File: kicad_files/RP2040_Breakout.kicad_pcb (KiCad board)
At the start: 2 copper layers, 20.8 x 52.3 mm, 4 parts, among them IC1 RPI_Chip_RP2040-10-10, IC3 W25Q128JVSIQ, J1 690-005-298-486, J2 Conn_02x20_Counter_Clockwise

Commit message: placement completed
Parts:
- added C1: 0.1uf, Capacitor_SMD:C_0201_0603Metric, F.Cu at (135.6, 95.6)
- added C10: 0.1uf, Capacitor_SMD:C_0201_0603Metric, F.Cu at (132.1, 97.9)
- added C11: 47uf, Capacitor_SMD:C_0805_2012Metric, F.Cu at (139.8, 90.1)
- added C12: 47uf, Capacitor_SMD:C_0805_2012Metric, F.Cu at (139.7, 84.3)
- added C13: 15pf, Capacitor_SMD:C_0201_0603Metric, F.Cu at (131.9, 109.5)
- added C14: 15pf, Capacitor_SMD:C_0201_0603Metric, F.Cu at (139.8, 108.5)
- added C15: 2u2, Capacitor_SMD:C_0201_0603Metric, F.Cu at (140.7, 95.6)
- added C16: 100nf, Capacitor_SMD:C_0201_0603Metric, F.Cu at (132.1, 91.8)
- added C17: 2u2, Capacitor_SMD:C_0402_1005Metric, F.Cu at (131.2, 92.0)
- added C18: 1nf, Capacitor_SMD:C_0402_1005Metric, F.Cu at (139.5, 93.8)
- added C2: 0.1uf, Capacitor_SMD:C_0201_0603Metric, F.Cu at (138.3, 105.8)
- added C3: 0.1uf, Capacitor_SMD:C_0201_0603Metric, F.Cu at (137.2, 95.6)
- added C4: 0.1uf, Capacitor_SMD:C_0201_0603Metric, F.Cu at (142.3, 97.9)
- added C5: 0.1uf, Capacitor_SMD:C_0201_0603Metric, F.Cu at (142.3, 101.5)
- added C6: 0.1uf, Capacitor_SMD:C_0201_0603Metric, F.Cu at (139.2, 105.8)
- added C7: 0.1uf, Capacitor_SMD:C_0201_0603Metric, F.Cu at (136.4, 95.6)
- added C8: 0.1uf, Capacitor_SMD:C_0201_0603Metric, F.Cu at (139.9, 95.6)
- added C9: 0.1uf, Capacitor_SMD:C_0201_0603Metric, F.Cu at (132.1, 101.5)
- added D1: MBR120VLSFT1G, SamacSys_Parts:SODFL3616X98N, F.Cu at (143.1, 82.9)
- added D2: LED_Small, LED_SMD:LED_0402_1005Metric, F.Cu at (131.7, 81.6)
- added G***: LOGO, footprints:logo2, F.Cu at (136.8, 117.3)
- added IC2: RT6150B-33GQW, SamacSys_Parts:SON50P250X250X80-11N-D, F.Cu at (139.4, 87.0)
- added J3: Conn_01x03_Pin, footprints:3Pin_Header, F.Cu at (137.1, 125.8)
- added L1: 2u2, SamacSys_Parts:DFE2016CKA1R0MP2, F.Cu at (142.8, 87.1)
- added Q1: DMG1012T-7, SamacSys_Parts:SOT50P160X80-3N, F.Cu at (142.4, 93.0)
- added R1: 5.6K, Resistor_SMD:R_0201_0603Metric, F.Cu at (142.5, 99.5)
- added R10: 1R, Resistor_SMD:R_0201_0603Metric, F.Cu at (141.6, 95.6)
- added R11: 200, Resistor_SMD:R_0201_0603Metric, F.Cu at (142.5, 95.6)
- added R12: 1K, Resistor_SMD:R_0201_0603Metric, F.Cu at (136.6, 83.5)
- added R13: DNP, Resistor_SMD:R_0201_0603Metric, F.Cu at (132.8, 95.5)
- added R14: 200K, Resistor_SMD:R_0201_0603Metric, F.Cu at (140.5, 92.2)
- added R15: 100K, Resistor_SMD:R_0201_0603Metric, F.Cu at (140.5, 93.7)
- added R2: 10K, Resistor_SMD:R_0201_0603Metric, F.Cu at (142.5, 100.3)
- added R3: 100K, Resistor_SMD:R_0201_0603Metric, F.Cu at (139.7, 81.8)
- added R4: 100K, Resistor_SMD:R_0201_0603Metric, F.Cu at (139.7, 82.6)
- added R5: 27, Resistor_SMD:R_0201_0603Metric, F.Cu at (138.1, 95.6)
- added R6: 27, Resistor_SMD:R_0201_0603Metric, F.Cu at (138.9, 95.6)
- added R7: R_Small, Resistor_SMD:R_0201_0603Metric, F.Cu at (135.6, 106.0)
- added R8: 1K, Resistor_SMD:R_0201_0603Metric, F.Cu at (137.1, 106.0)
- added R9: 470, Resistor_SMD:R_0402_1005Metric, F.Cu at (133.8, 81.6)
- added REF**: CE-Logo_8.5x6mm_SilkScreen, Symbol:CE-Logo_8.5x6mm_SilkScreen, B.Cu at (137.1, 105.5)
- added REF**: FCC-Logo_7.3x6mm_SilkScreen, Symbol:FCC-Logo_7.3x6mm_SilkScreen, B.Cu at (136.6, 113.8)
- added S1: PTS815_SJM_250_SMTR_LFS, SamacSys_Parts:PTS815SJM250SMTRLFS, F.Cu at (133.2, 86.4)
- added TP1: , footprints:Custom_testpad, B.Cu at (139.4, 83.1)
- added TP2: , footprints:Custom_testpad, B.Cu at (139.4, 85.4)
- added TP3: , footprints:Custom_testpad, B.Cu at (139.4, 87.8)
- added TP4: , footprints:Custom_testpad, B.Cu at (139.4, 90.1)
- added TP5: , footprints:Custom_testpad, B.Cu at (134.6, 83.1)
- added TP6: , footprints:Custom_testpad, B.Cu at (134.6, 85.4)
- added Y1: Crystal_GND23, SamacSys_Parts:YSX321SL, F.Cu at (136.4, 109.0)
- IC3: value W25Q128JVSIQ -> W25Q16JVUXIQ_TR; footprint SamacSys_Parts:SOIC127P790X216-8N -> SamacSys_Parts:SON50P300X200X60-9N
- moved IC3 43.1 mm to (133.9, 92.9), turned to 90 degrees
- moved IC1 2.64 mm to (137.1, 100.5)
- moved J1 1.15 mm to (137.1, 76.9)
- moved J2 0.65 mm to (137.1, 100.5)
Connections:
- IC3 pad 1: unconnected-(IC3-/CS-Pad1) -> /rp2040/QSPI_SS_N
- IC3 pad 2: unconnected-(IC3-DO_(IO1)-Pad2) -> /rp2040/QSPI_SD1
- IC3 pad 3: unconnected-(IC3-/WP_(IO2)-Pad3) -> /rp2040/QSPI_SD2
- IC3 pad 4: unconnected-(IC3-GND-Pad4) -> GND
- IC3 pad 5: unconnected-(IC3-DI_(IO0)-Pad5) -> /rp2040/QSPI_SD0
- IC3 pad 6: unconnected-(IC3-CLK-Pad6) -> /rp2040/QSPI_SCLK
- IC3 pad 7: unconnected-(IC3-/HOLD_OR_/RESET_(IO3)-Pad7) -> /rp2040/QSPI_SD3
- IC3 pad 8: unconnected-(IC3-VCC-Pad8) -> /rp2040/IOVDD_1
- J1 pad SH1: (no net) -> GND
- J1 pad SH2: (no net) -> GND
- J1 pad SH3: (no net) -> GND
- J1 pad SH4: (no net) -> GND
- J1 pad SH5: (no net) -> GND
- J1 pad SH6: (no net) -> GND
- J2 pad 36: /power_chain/3V3 -> /rp2040/IOVDD_1
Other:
- board size 20.8 x 52.3 mm -> 21 x 52.3 mm

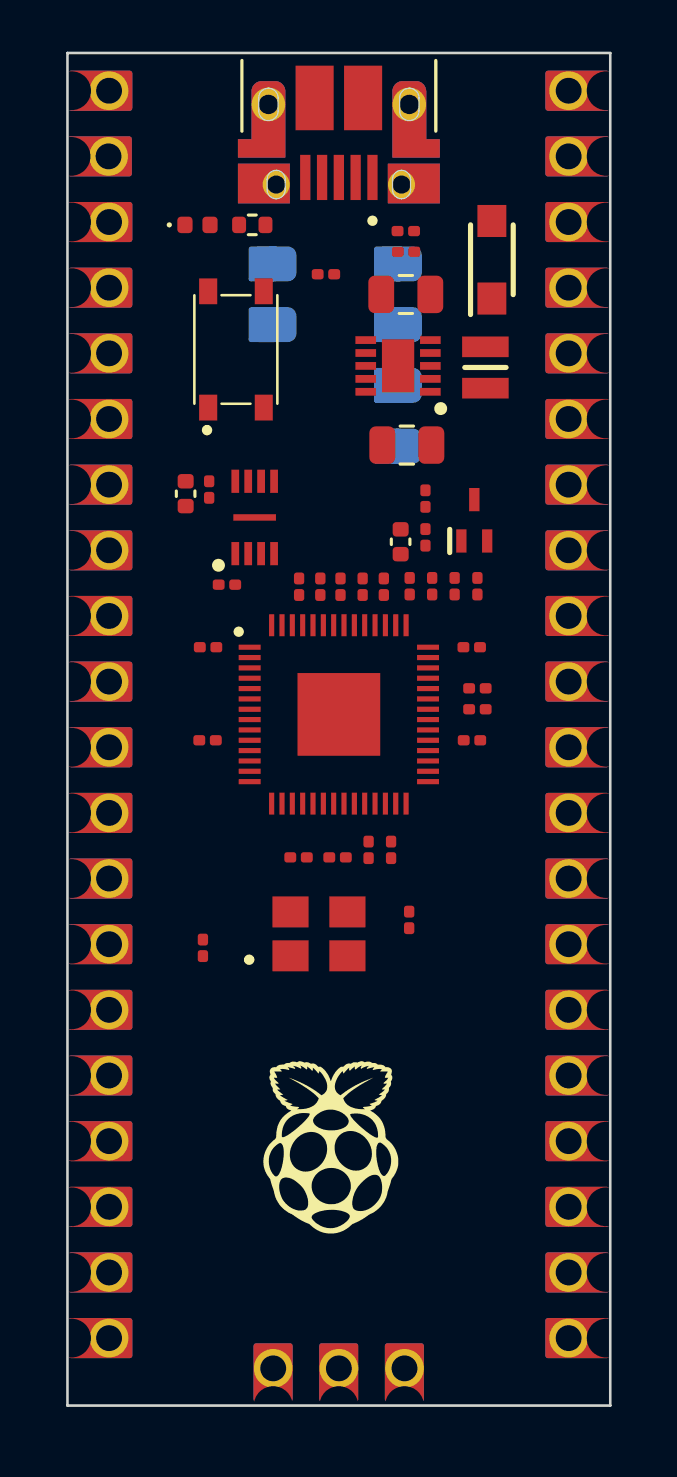
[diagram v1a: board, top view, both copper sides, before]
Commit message: initial routing started
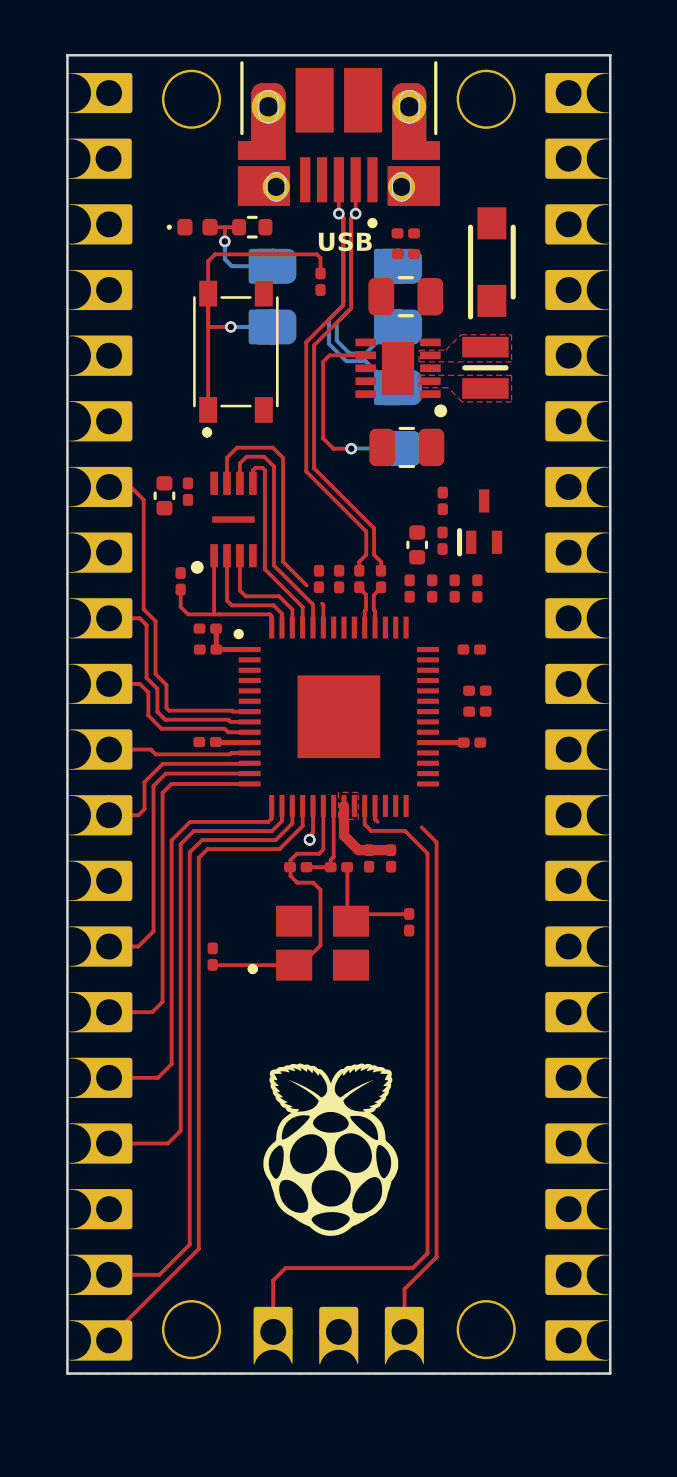
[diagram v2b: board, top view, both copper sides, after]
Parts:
- removed REF**: CE-Logo_8.5x6mm_SilkScreen, Symbol:CE-Logo_8.5x6mm_SilkScreen
- removed REF**: FCC-Logo_7.3x6mm_SilkScreen, Symbol:FCC-Logo_7.3x6mm_SilkScreen
- added H1: MountingHole, footprints:Mounting_Hole, F.Cu at (131.4, 76.7)
- added H2: MountingHole, footprints:Mounting_Hole, F.Cu at (142.8, 76.7)
- added H3: MountingHole, footprints:Mounting_Hole, F.Cu at (131.4, 124.3)
- added H4: MountingHole, footprints:Mounting_Hole, F.Cu at (142.8, 124.3)
- moved C1 3.89 mm to (132.1, 97.2), turned to 180 degrees
- moved R13 1.79 mm to (131.0, 95.4), turned to 90 degrees
- moved J3 1.41 mm to (137.1, 124.4)
- moved C16 0.82 mm to (131.3, 91.9)
- moved C17 0.82 mm to (130.4, 92.1)
- moved IC3 0.82 mm to (133.1, 93.0)
- moved R14 0.68 mm to (141.2, 92.3)
- moved R15 0.67 mm to (141.1, 93.8)
- moved C18 0.65 mm to (140.2, 94.0)
- moved C13 0.51 mm to (132.2, 109.9)
- moved Y1 0.39 mm to (136.5, 109.4)
- moved R8 0.38 mm to (137.1, 106.4)
- moved Q1 0.38 mm to (142.8, 93.1)
- moved R7 0.38 mm to (135.6, 106.4)
- moved R12 0.36 mm to (136.4, 83.8), turned to 90 degrees
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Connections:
- C1 pad 1: /rp2040/IOVDD_1 -> /rp2040/DVDD_1
- C10 pad 1: /rp2040/IOVDD_1 -> /rp2040/DVDD_1
- C11 pad 1: /rp2040/IOVDD_1 -> /rp2040/DVDD_1
- C16 pad 1: /rp2040/IOVDD_1 -> /rp2040/DVDD_1
- C17 pad 1: /rp2040/IOVDD_1 -> /rp2040/DVDD_1
- C2 pad 1: /rp2040/IOVDD_1 -> /rp2040/DVDD_1
- C3 pad 1: /rp2040/IOVDD_1 -> /rp2040/DVDD_1
- C4 pad 1: /rp2040/IOVDD_1 -> /rp2040/DVDD_1
- C5 pad 1: /rp2040/IOVDD_1 -> /rp2040/DVDD_1
- C6 pad 1: /rp2040/IOVDD_1 -> /rp2040/DVDD_1
- C7 pad 1: /rp2040/IOVDD_1 -> /rp2040/DVDD_1
- C8 pad 1: /rp2040/IOVDD_1 -> /rp2040/DVDD_1
- C9 pad 1: /rp2040/IOVDD_1 -> /rp2040/DVDD_1
- IC1 pad 1: /rp2040/IOVDD_1 -> /rp2040/DVDD_1
- IC1 pad 10: /rp2040/IOVDD_1 -> /rp2040/DVDD_1
- IC1 pad 22: /rp2040/IOVDD_1 -> /rp2040/DVDD_1
- IC1 pad 33: /rp2040/IOVDD_1 -> /rp2040/DVDD_1
- IC1 pad 42: /rp2040/IOVDD_1 -> /rp2040/DVDD_1
- IC1 pad 44: /rp2040/IOVDD_1 -> /rp2040/DVDD_1
- IC1 pad 46: /power_chain/USB_DM -> /rp2040/USB_D-
- IC1 pad 47: /power_chain/USB_DP -> /rp2040/USB_D+
- IC1 pad 48: /rp2040/IOVDD_1 -> /rp2040/DVDD_1
- IC1 pad 49: /rp2040/IOVDD_1 -> /rp2040/DVDD_1
- IC1 pad 50: /rp2040/DVDD_2 -> /rp2040/DVDD_1
- IC2 pad 1: /rp2040/IOVDD_1 -> /rp2040/DVDD_1
- IC2 pad 10: /rp2040/IOVDD_1 -> /rp2040/DVDD_1
- IC3 pad 8: /rp2040/IOVDD_1 -> /rp2040/DVDD_1
- J1 pad 2: /power_chain/USB_DM -> /power_chain/USB_D-
- J1 pad 3: /power_chain/USB_DP -> /power_chain/USB_D+
- J2 pad 36: /rp2040/IOVDD_1 -> /rp2040/DVDD_1
- J3 pad 1: /rp2040/SWDIO -> /rp2040/SWCLK
- J3 pad 3: /rp2040/SWCLK -> /rp2040/SWDIO
- Q1 pad 1: /rp2040/IOVDD_1 -> /rp2040/DVDD_1
- R11 pad 1: /rp2040/IOVDD_1 -> /rp2040/DVDD_1
- R13 pad 2: /rp2040/IOVDD_1 -> /rp2040/DVDD_1
- R5 pad 1: /power_chain/USB_DP -> /power_chain/USB_D+
- R5 pad 2: /power_chain/USB_DP -> /rp2040/USB_D+
- R6 pad 1: /power_chain/USB_DM -> /power_chain/USB_D-
- R6 pad 2: /power_chain/USB_DM -> /rp2040/USB_D-
- TP2 pad 1: /power_chain/USB_DM -> /power_chain/USB_D-
- TP3 pad 1: /power_chain/USB_DP -> /power_chain/USB_D+
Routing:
- net /rp2040/SWCLK: track 0.00 -> 27.5 mm
- net /power_chain/USB_D+: track 0.00 -> 25.6 mm, vias 0 -> 1
- net /rp2040/GPIO15: track 0.00 -> 25.4 mm
- net /power_chain/USB_D-: track 0.00 -> 25.1 mm, vias 0 -> 1
- net /rp2040/GPIO14: track 0.00 -> 23.9 mm
- net /rp2040/SWDIO: track 0.00 -> 21.0 mm
- net /rp2040/GPIO13: track 0.00 -> 18.9 mm
- net /rp2040/GPIO12: track 0.00 -> 16.0 mm
- net Net-(S1-COM_1): track 0.00 -> 14.7 mm, vias 0 -> 1
- net /rp2040/GPIO11: track 0.00 -> 13.8 mm
- net /rp2040/GPIO5: track 0.00 -> 13.2 mm
- net /rp2040/GPIO10: track 0.00 -> 11.5 mm
- net /rp2040/XIN: track 0.00 -> 11.3 mm
- net /rp2040/QSPI_SD3: track 0.00 -> 9.75 mm
- net /rp2040/QSPI_SCLK: track 0.00 -> 9.21 mm
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- added copper zone on F.Cu, net /rp2040/DVDD_1
- added copper zone on B.Cu, net GND
- added copper zone on F.Cu, net GND
- added copper zone on F.Cu, net Net-(IC2-LX1)
- added copper zone on F.Cu, net Net-(IC2-LX2)
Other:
- board size 21 x 52.3 mm -> 21 x 51 mm
- board text added: "USB"

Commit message: routing progess
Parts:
- moved R4 9.17 mm to (138.8, 91.8)
- moved C17 1.30 mm to (131.2, 93.1)
- moved R3 1.14 mm to (140.4, 82.8)
- moved C14 1.05 mm to (139.9, 109.6)
- moved Y1 0.74 mm to (136.6, 110.1)
- moved C13 0.74 mm to (132.2, 110.6)
- moved R7 0.72 mm to (135.6, 107.2)
- moved R8 0.72 mm to (137.1, 107.2)
- moved C6 0.65 mm to (139.1, 106.7)
- moved C2 0.65 mm to (138.3, 106.7)
- moved C16 0.55 mm to (131.3, 91.3), turned to 90 degrees
- moved R1 0.41 mm to (142.3, 100.0)
- moved R13 0.39 mm to (131.3, 95.6), turned to 180 degrees
- moved R2 0.36 mm to (142.3, 100.7)
- moved J2 0.09 mm to (137.1, 100.5)
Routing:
- net /rp2040/DVDD_1: track 8.01 -> 77.8 mm, vias 0 -> 15
- net /rp2040/GPIO16: track 0.00 -> 25.1 mm
- net /rp2040/GPIO25: track 0.00 -> 24.0 mm, vias 0 -> 2
- net /rp2040/GPIO17: track 0.00 -> 22.8 mm
- net /rp2040/GPIO2: track 0.00 -> 19.6 mm
- net /rp2040/GPIO18: track 0.00 -> 18.5 mm
- net /rp2040/GPIO3: track 0.00 -> 17.6 mm
- net /rp2040/GPIO23: track 7.80 -> 25.2 mm, vias 1 -> 2
- net /power_chain/VSYS: track 0.00 -> 16.6 mm
- net /rp2040/GPIO19: track 0.00 -> 16.3 mm
- net /rp2040/GPIO4: track 0.00 -> 15.5 mm
- net /power_chain/3V3_EN: track 0.00 -> 15.2 mm, vias 0 -> 1
- net /rp2040/GPIO20: track 0.00 -> 14.2 mm
- net /rp2040/QSPI_SS_N: track 7.05 -> 20.8 mm, vias 0 -> 2
- net /power_chain/VBUS: track 0.00 -> 12.8 mm
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- added copper zone on F.Cu, net /power_chain/VSYS

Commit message: routing completed
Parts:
- added kibuzzard-65E013B1: G***, kibuzzard-65E013B1, B.Cu at (142.9, 78.7)
- added kibuzzard-65E014B1: G***, kibuzzard-65E014B1, B.Cu at (131.1, 79.9)
- added kibuzzard-65E014B1: G***, kibuzzard-65E014B1, B.Cu at (131.1, 81.5)
- added kibuzzard-65E014B1: G***, kibuzzard-65E014B1, B.Cu at (131.1, 78.6)
- added kibuzzard-65E01689: G***, kibuzzard-65E01689, B.Cu at (142.9, 80.0)
- added kibuzzard-65E01690: G***, kibuzzard-65E01690, B.Cu at (142.9, 81.4)
- added kibuzzard-65E01696: G***, kibuzzard-65E01696, B.Cu at (142.9, 83.8)
- added kibuzzard-65E0169F: G***, kibuzzard-65E0169F, B.Cu at (142.9, 86.5)
- added kibuzzard-65E016BD: G***, kibuzzard-65E016BD, B.Cu at (143.0, 89.1)
- added kibuzzard-65E016CF: G***, kibuzzard-65E016CF, B.Cu at (142.9, 91.6)
- added kibuzzard-65E016D7: G***, kibuzzard-65E016D7, B.Cu at (142.0, 94.2)
- added kibuzzard-65E01F49: G***, kibuzzard-65E01F49, B.Cu at (142.9, 96.8)
- added kibuzzard-65E01F54: G***, kibuzzard-65E01F54, B.Cu at (142.9, 99.3)
- added kibuzzard-65E01F60: G***, kibuzzard-65E01F60, B.Cu at (143.0, 102.0)
- added kibuzzard-65E01F69: G***, kibuzzard-65E01F69, B.Cu at (143.0, 104.2)
- added kibuzzard-65E01F72: G***, kibuzzard-65E01F72, B.Cu at (143.0, 106.9)
- added kibuzzard-65E01F7B: G***, kibuzzard-65E01F7B, B.Cu at (143.0, 109.4)
- added kibuzzard-65E01F83: G***, kibuzzard-65E01F83, B.Cu at (143.0, 112.0)
- added kibuzzard-65E01F8B: G***, kibuzzard-65E01F8B, B.Cu at (143.0, 114.5)
- added kibuzzard-65E01F93: G***, kibuzzard-65E01F93, B.Cu at (143.0, 117.1)
- added kibuzzard-65E01F9A: G***, kibuzzard-65E01F9A, B.Cu at (143.1, 119.4)
- added kibuzzard-65E01FA3: G***, kibuzzard-65E01FA3, B.Cu at (143.1, 120.7)
- added kibuzzard-65E01FAC: G***, kibuzzard-65E01FAC, B.Cu at (137.2, 121.7)
- added kibuzzard-65E01FAC: G***, kibuzzard-65E01FAC, B.Cu at (143.1, 122.0)
- added kibuzzard-65E01FDC: G***, kibuzzard-65E01FDC, B.Cu at (139.7, 121.1)
- added kibuzzard-65E01FEF: G***, kibuzzard-65E01FEF, B.Cu at (134.6, 121.0)
- moved C10 0.14 mm to (132.1, 97.9)
- moved C1 0.10 mm to (132.1, 97.1)
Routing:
- net /rp2040/GPIO0: track 0.73 -> 25.6 mm, vias 0 -> 1
- net /rp2040/GPIO1: track 1.66 -> 24.4 mm
- net /power_chain/VBUS: track 12.8 -> 34.0 mm, vias 0 -> 4
- net /power_chain/VSYS: track 16.6 -> 34.4 mm, vias 0 -> 3
- net /rp2040/DVDD_1: track 77.8 -> 77.1 mm
- net GND: vias 61 -> 58

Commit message: back side screen updated
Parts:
- added kibuzzard-65E014B1: G***, kibuzzard-65E014B1, B.Cu at (131.0, 119.5)
- added kibuzzard-65E014B1: G***, kibuzzard-65E014B1, B.Cu at (131.1, 84.0)
- added kibuzzard-65E014B1: G***, kibuzzard-65E014B1, B.Cu at (131.0, 109.3)
- added kibuzzard-65E014B1: G***, kibuzzard-65E014B1, B.Cu at (131.1, 99.2)
- added kibuzzard-65E014B1: G***, kibuzzard-65E014B1, B.Cu at (131.0, 117.0)
- added kibuzzard-65E014B1: G***, kibuzzard-65E014B1, B.Cu at (131.1, 104.2)
- added kibuzzard-65E014B1: G***, kibuzzard-65E014B1, B.Cu at (131.0, 114.5)
- added kibuzzard-65E014B1: G***, kibuzzard-65E014B1, B.Cu at (131.1, 96.7)
- added kibuzzard-65E014B1: G***, kibuzzard-65E014B1, B.Cu at (131.1, 101.7)
- added kibuzzard-65E014B1: G***, kibuzzard-65E014B1, B.Cu at (131.0, 106.8)
- added kibuzzard-65E014B1: G***, kibuzzard-65E014B1, B.Cu at (131.1, 94.2)
- added kibuzzard-65E014B1: G***, kibuzzard-65E014B1, B.Cu at (131.1, 86.5)
- added kibuzzard-65E014B1: G***, kibuzzard-65E014B1, B.Cu at (131.1, 91.7)
- added kibuzzard-65E014B1: G***, kibuzzard-65E014B1, B.Cu at (131.0, 112.0)
- added kibuzzard-65E014B1: G***, kibuzzard-65E014B1, B.Cu at (131.1, 89.1)
- added kibuzzard-65E04185: G***, kibuzzard-65E04185, B.Cu at (130.9, 122.1)
- added kibuzzard-65E0419F: G***, kibuzzard-65E0419F, B.Cu at (130.9, 120.8)

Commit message: output file generated
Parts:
- removed the kibuzzard-65E014B1 at (131.1, 79.9)
- removed the kibuzzard-65E014B1 at (131.1, 78.6)
- removed the kibuzzard-65E014B1 at (131.1, 84.0)
- removed the kibuzzard-65E014B1 at (131.0, 109.3)
- removed the kibuzzard-65E014B1 at (131.1, 99.2)
- removed the kibuzzard-65E014B1 at (131.0, 117.0)
- removed the kibuzzard-65E014B1 at (131.1, 104.2)
- removed the kibuzzard-65E014B1 at (131.0, 114.5)
- removed the kibuzzard-65E014B1 at (131.1, 96.7)
- removed the kibuzzard-65E014B1 at (131.1, 86.5)
- removed the kibuzzard-65E014B1 at (131.1, 91.7)
- removed the kibuzzard-65E014B1 at (131.0, 112.0)
- removed the kibuzzard-65E014B1 at (131.1, 89.1)
- added REF**: WEEE-Logo_4.2x6mm_SilkScreen, Symbol:WEEE-Logo_4.2x6mm_SilkScreen, B.Cu at (136.5, 115.9)
- added REF**: CE-Logo_8.5x6mm_SilkScreen, Symbol:CE-Logo_8.5x6mm_SilkScreen, B.Cu at (137.1, 108.6)
- added kibuzzard-65E0730F: G***, kibuzzard-65E0730F, B.Cu at (131.0, 117.0)
- added kibuzzard-65E07316: G***, kibuzzard-65E07316, B.Cu at (131.0, 114.5)
- added kibuzzard-65E0731E: G***, kibuzzard-65E0731E, B.Cu at (131.0, 112.0)
- added kibuzzard-65E07326: G***, kibuzzard-65E07326, B.Cu at (131.0, 109.3)
- added kibuzzard-65E07330: G***, kibuzzard-65E07330, B.Cu at (131.1, 104.2)
- added kibuzzard-65E0733A: G***, kibuzzard-65E0733A, B.Cu at (131.1, 99.2)
- added kibuzzard-65E07341: G***, kibuzzard-65E07341, B.Cu at (131.1, 96.7)
- added kibuzzard-65E07348: G***, kibuzzard-65E07348, B.Cu at (131.1, 91.7)
- added kibuzzard-65E07350: G***, kibuzzard-65E07350, B.Cu at (131.1, 89.1)
- added kibuzzard-65E07397: G***, kibuzzard-65E07397, B.Cu at (131.1, 86.5)
- added kibuzzard-65E0739D: G***, kibuzzard-65E0739D, B.Cu at (131.1, 84.0)
- added kibuzzard-65E073A5: G***, kibuzzard-65E073A5, B.Cu at (131.1, 79.9)
- added kibuzzard-65E073AB: G***, kibuzzard-65E073AB, B.Cu at (131.1, 78.6)
- moved kibuzzard-65E013B1 0.06 mm to (142.9, 78.7)
